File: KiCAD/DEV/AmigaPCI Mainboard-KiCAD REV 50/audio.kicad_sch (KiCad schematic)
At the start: 65 parts, among them CN500 DSP/DVD (RGGL), CN501 AudioJack, Q500 MMBFJ211, Q501 MMBFJ211, Q502 MMBT3906, U220 74LVC08, U500 8364, U501 LF347, U502 LM833

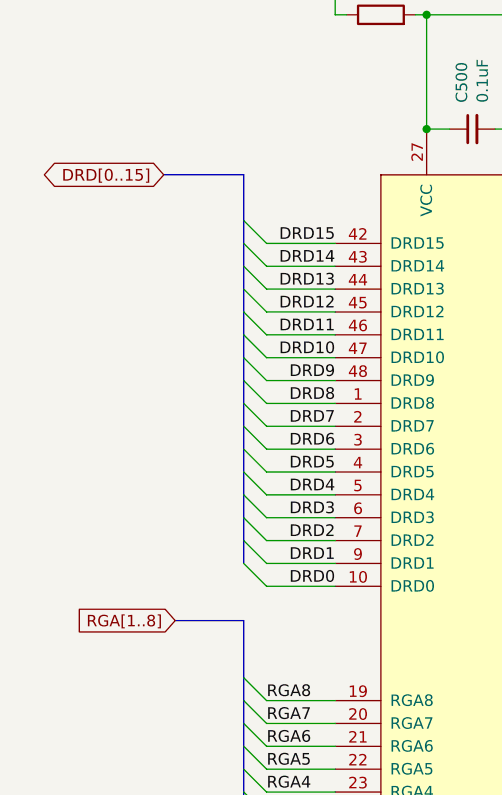
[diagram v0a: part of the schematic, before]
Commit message: Updated STM32F205 microcontroller.
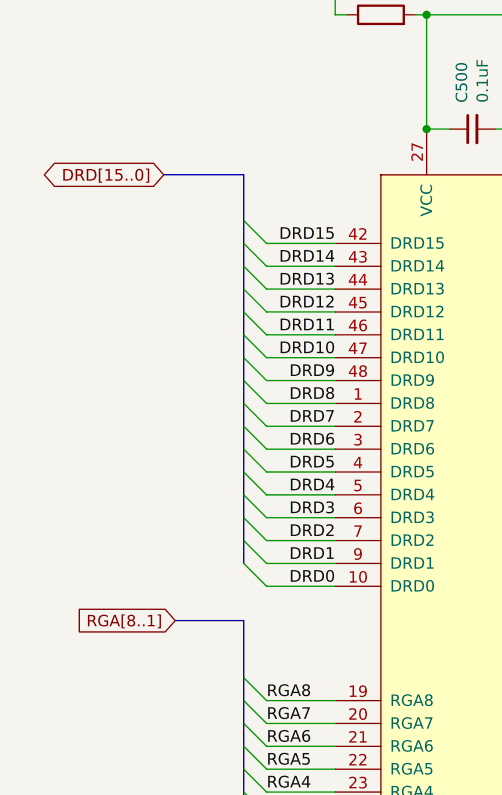
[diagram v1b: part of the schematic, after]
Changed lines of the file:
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@@
 		)
 	)
-	(global_label "DRD[0..15]"
+	(global_label "DRD[15..0]"
 		(shape bidirectional)
 		(at 52.07 50.8 180)
@@
 		)
 	)
-	(global_label "RGA[1..8]"
+	(global_label "RGA[8..1]"
 		(shape input)
 		(at 53.34 100.33 180)
